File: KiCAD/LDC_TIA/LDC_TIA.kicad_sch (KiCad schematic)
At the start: 19 parts, among them J1 Conn_01x02_Pin, J2 Conn_01x06_Pin, J3 54-00166, Q1 BC817, SW1 SW_SPST, U1 OPA2197xDGK, U2 LM7805_TO220

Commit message: Initial Commit
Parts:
- J3: footprint JACK:TENSILITY_54-00166 -> Footprints:TENSILITY_54-00166
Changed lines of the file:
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@@
 			)
 		)
-		(property "Footprint" "JACK:TENSILITY_54-00166"
+		(property "Footprint" "Footprints:TENSILITY_54-00166"
 			(at 91.44 107.95 0)
 			(effects

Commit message: Done with Schematics V1
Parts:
- removed C1, C2: 10pF, Capacitor_SMD:C_0201_0603Metric, symbol Library:C
- removed C4: 0.33uF, Capacitor_SMD:C_0201_0603Metric, symbol Library:C
- removed C5: 0.1uF, Capacitor_SMD:C_0201_0603Metric, symbol Library:C
- removed J2: Conn_01x06_Pin, Connector_PinHeader_2.54mm:PinHeader_1x06_P2.54mm_Vertical, symbol Connector:Conn_01x06_Pin
- removed J3: 54-00166, Footprints:TENSILITY_54-00166, symbol Library:54-00166
- removed Q1: BC817, Package_TO_SOT_SMD:SOT-23, symbol Library:BC817
- removed R1: 2K, Resistor_THT:R_Axial_DIN0207_L6.3mm_D2.5mm_P7.62mm_Horizontal, symbol Library:R
- removed R2: 1K, Resistor_THT:R_Axial_DIN0207_L6.3mm_D2.5mm_P7.62mm_Horizontal, symbol Library:R
- removed R3: 62, Resistor_THT:R_Axial_DIN0309_L9.0mm_D3.2mm_P25.40mm_Horizontal, symbol Library:R
- removed R4, R5: 2k, Resistor_THT:R_Axial_DIN0204_L3.6mm_D1.6mm_P5.08mm_Horizontal, symbol Library:R
- removed SW1: SW_SPST, symbol Switch:SW_SPST
- removed U1: OPA2197xDGK, Package_SO:VSSOP-8_3x3mm_P0.65mm, symbol Library:OPA2197xDGK
- added C1: 0.1UF, FOOTPRINTS:CAP_UEP_5X11_NCH, symbol Device:C
- added C2, C7: 10pF, FOOTPRINTS:CAPRB250W50L400T250H550, symbol Device:C
- added C3, C6: 10pF, FOOTPRINTS:CAPRB250W50L400T250H550, symbol Device:C_Polarized_Small_US
- added C5: 0.33uF, FOOTPRINTS:CAP_UEP_5X11_NCH, symbol Device:C
- added J2: 54-00166, FOOTPRINTS:TENSILITY_54-00166, symbol 54-00166:54-00166
- added J5: Conn_01x07_Pin, Connector_PinHeader_2.54mm:PinHeader_1x07_P2.54mm_Vertical, symbol Connector:Conn_01x07_Pin
- added Q1: BC817, Package_TO_SOT_SMD:SOT-23, symbol potentiometer:BC817
- added R1: 2k, Resistor_THT:R_Axial_DIN0207_L6.3mm_D2.5mm_P7.62mm_Horizontal, symbol Device:R
- added R2: 1k, Resistor_THT:R_Axial_DIN0207_L6.3mm_D2.5mm_P7.62mm_Horizontal, symbol Device:R
- added R3: 62, Resistor_THT:R_Axial_DIN0309_L9.0mm_D3.2mm_P12.70mm_Horizontal, symbol Device:R
- added R4: 2K, Resistor_THT:R_Axial_DIN0207_L6.3mm_D2.5mm_P7.62mm_Horizontal, symbol potentiometer:R
- added R5: 2K, Resistor_THT:R_Axial_DIN0207_L6.3mm_D2.5mm_P7.62mm_Horizontal, symbol Device:R
- added S1: GPTS203211B, FOOTPRINTS:GPTS203211B, symbol GPTS203211B:GPTS203211B
- added U3: OPA2197xD, Package_SO:SOIC-8_3.9x4.9mm_P1.27mm, symbol Amplifier_Operational:OPA2197xD
- added U4: LTC1044, FOOTPRINTS:PDIP-8_N_LIT, symbol Regulator_SwitchedCapacitor:LTC1044
- RV1: footprint (none) -> FOOTPRINTS:potentiometer
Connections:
- net +VCC: now also C1.1, S1.1, U3.8 (V+), U4.8 (V+)
- net ANODE: now also J5.2 (Pin_2)
- net CATHODE: now also C2.1, J5.1 (Pin_1), R5.1, U3.6 (-)
- net GND: now also C1.2, C5.2, C6.1, C7.2, J2.B, J2.C, J5.6 (Pin_6), J5.7 (Pin_7), R1.2, R3.2, R4.2, U4.3 (GND)
- net VI: now also C5.1, J2.A
- net VOUT: now also C2.2, J5.3 (Pin_3), R5.2, U3.7
- net VR: now also J5.4 (Pin_4)
- net at D1.2 (A): now also S1.2
- net at J1.2 (Pin_2): now also Q1.3 (C)
- net at RV1.2: now also U3.3 (+)
- new net: Q1.2 (E), R2.2, R3.1
- new net: C7.1, R4.1, U3.5 (+)
- new net: Q1.1 (B), U3.1
- new net: C3.1, U4.2 (CAP+)
- new net: C3.2, U4.4 (CAP-)
- new net: R1.1, R2.1, U3.2 (-)
- new net -VCC: C6.2, J5.5 (Pin_5), U3.4 (V-), U4.5 (VOUT)
- no-connect marks 0 -> 3
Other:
- moved on the sheet: D1, J1, JP1, RV1, U2

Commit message: PCB layout
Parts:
- J3: renamed from J1; footprint Connector_Samtec_HPM_THT:Samtec_HPM-02-01-x-S_Straight_1x02_Pitch5.08mm -> Connector_PinHeader_2.54mm:PinHeader_1x02_P2.54mm_Vertical
- renumbered C7 to C1, C5 to C3, C3 to C4, C1 to C5, J2 to J1, J5 to J2, R4 to R1, R5 to R2, R1 to R3, R2 to R4, R3 to R5, U3 to U1, U4 to U2, U2 to U3
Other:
- moved on the sheet: U1C
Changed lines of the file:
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@@
 	)
 	(rectangle
-		(start 114.808 123.444)
-		(end 146.05 154.94)
+		(start 113.538 124.714)
+		(end 144.78 156.21)
 		(stroke
 			(width 0)
@@
 	)
 	(label "-VCC"
-		(at 128.27 144.78 270)
+		(at 127 146.05 270)
 		(effects
 			(font
@@
 	)
 	(label "+VCC"
-		(at 128.27 129.54 90)
+		(at 127 130.81 90)
 		(effects
 			(font
@@
 		(dnp no)
 		(fields_autoplaced yes)
-		(property "Reference" "#PWR04"
+		(property "Reference" "#PWR03"
 			(at 128.27 105.41 0)
 			(effects
@@
 			(project ""
 				(path "/c2e64472-a533-4958-9229-ae3f836cc80a"
-					(reference "#PWR04")
+					(reference "#PWR03")
 					(unit 1)
 				)
@@
 		(on_board yes)
 		(dnp no)
-		(property "Reference" "J5"
+		(property "Reference" "J2"
 			(at 166.37 125.73 0)
 			(effects
@@
 			(project ""
 				(path "/c2e64472-a533-4958-9229-ae3f836cc80a"
-					(reference "J5")
+					(reference "J2")
 					(unit 1)
 				)
@@
 		(dnp no)
 		(fields_autoplaced yes)
-		(property "Reference" "R3"
+		(property "Reference" "R5"
 			(at 266.7 99.0599 0)
 			(effects
@@
 			(project ""
 				(path "/c2e64472-a533-4958-9229-ae3f836cc80a"
-					(reference "R3")
+					(reference "R5")
 					(unit 1)
 				)
@@
 		(dnp no)
 		(fields_autoplaced yes)
-		(property "Reference" "C7"
+		(property "Reference" "C1"
 			(at 45.72 64.7699 0)
 			(effects
@@
 			(project ""
 				(path "/c2e64472-a533-4958-9229-ae3f836cc80a"
-					(reference "C7")
+					(reference "C1")
 					(unit 1)
 				)
@@
 		(dnp no)
 		(fields_autoplaced yes)
-		(property "Reference" "R5"
+		(property "Reference" "R2"
 			(at 74.93 71.12 90)
 			(effects
@@
 			(project ""
 				(path "/c2e64472-a533-4958-9229-ae3f836cc80a"
-					(reference "R5")
+					(reference "R2")
 					(unit 1)
 				)
@@
 		(on_board yes)
 		(dnp no)
-		(property "Reference" "C5"
+		(property "Reference" "C3"
 			(at 123.19 60.96 0)
 			(effects
@@
 			(project ""
 				(path "/c2e64472-a533-4958-9229-ae3f836cc80a"
-					(reference "C5")
+					(reference "C3")
 					(unit 1)
 				)
@@
 		(dnp no)
 		(fields_autoplaced yes)
-		(property "Reference" "C3"
+		(property "Reference" "C4"
 			(at 148.59 85.9281 0)
 			(effects
@@
 			(project ""
 				(path "/c2e64472-a533-4958-9229-ae3f836cc80a"
-					(reference "C3")
+					(reference "C4")
 					(unit 1)
 				)
@@
 		(on_board yes)
 		(dnp no)
-		(property "Reference" "J1"
+		(property "Reference" "J3"
 			(at 259.08 67.31 0)
 			(effects
@@
 			)
 		)
-		(property "Footprint" "Connector_Samtec_HPM_THT:Samtec_HPM-02-01-x-S_Straight_1x02_Pitch5.08mm"
+		(property "Footprint" "Connector_PinHeader_2.54mm:PinHeader_1x02_P2.54mm_Vertical"
 			(at 259.08 73.66 0)
 			(effects
@@
 			(project ""
 				(path "/c2e64472-a533-4958-9229-ae3f836cc80a"
-					(reference "J1")
+					(reference "J3")
 					(unit 1)
 				)
@@
 		(dnp no)
 		(fields_autoplaced yes)
-		(property "Reference" "#PWR03"
+		(property "Reference" "#PWR06"
 			(at 207.01 88.9 0)
 			(effects
@@
 			(project ""
 				(path "/c2e64472-a533-4958-9229-ae3f836cc80a"
-					(reference "#PWR03")
+					(reference "#PWR06")
 					(unit 1)
 				)
@@
 		(dnp no)
 		(fields_autoplaced yes)
-		(property "Reference" "#FLG02"
+		(property "Reference" "#FLG01"
 			(at 123.825 57.15 0)
 			(effects
@@
 			(project ""
 				(path "/c2e64472-a533-4958-9229-ae3f836cc80a"
-					(reference "#FLG02")
+					(reference "#FLG01")
 					(unit 1)
 				)
@@
 		(dnp no)
 		(fields_autoplaced yes)
-		(property "Reference" "U3"
+		(property "Reference" "U1"
 			(at 237.49 71.12 0)
 			(effects
@@
 			(project ""
 				(path "/c2e64472-a533-4958-9229-ae3f836cc80a"
-					(reference "U3")
+					(reference "U1")
 					(unit 1)
 				)
@@
 		(dnp no)
 		(fields_autoplaced yes)
-		(property "Reference" "#PWR06"
+		(property "Reference" "#PWR04"
 			(at 139.7 71.12 0)
 			(effects
@@
 			(project ""
 				(path "/c2e64472-a533-4958-9229-ae3f836cc80a"
-					(reference "#PWR06")
+					(reference "#PWR04")
 					(unit 1)
 				)
@@
 	(symbol
 		(lib_id "Amplifier_Operational:OPA2197xD")
-		(at 128.27 137.16 0)
+		(at 127 138.43 0)
 		(unit 3)
 		(exclude_from_sim no)
@@
 		(dnp no)
 		(fields_autoplaced yes)
-		(property "Reference" "U3"
-			(at 129.54 135.8899 0)
+		(property "Reference" "U1"
+			(at 128.27 137.1599 0)
 			(effects
 				(font
@@
 		)
 		(property "Value" "OPA2197xD"
-			(at 129.54 138.4299 0)
+			(at 128.27 139.6999 0)
 			(effects
 				(font
@@
 		)
 		(property "Footprint" "Package_SO:SOIC-8_3.9x4.9mm_P1.27mm"
-			(at 130.81 137.16 0)
+			(at 129.54 138.43 0)
 			(effects
 				(font
@@
 		)
 		(property "Datasheet" "http://www.ti.com/lit/ds/symlink/opa2197.pdf"
-			(at 134.62 133.35 0)
+			(at 133.35 134.62 0)
 			(effects
 				(font
@@
 		)
 		(property "Description" "Dual 36V, Precision, Rail-to-Rail Input/Output, Low Offset Voltage, Operational Amplifier, SOIC-8"
-			(at 128.27 137.16 0)
+			(at 127 138.43 0)
 			(effects
 				(font
@@
 			(project ""
 				(path "/c2e64472-a533-4958-9229-ae3f836cc80a"
-					(reference "U3")
+					(reference "U1")
 					(unit 3)
 				)
@@
 		(dnp no)
 		(fields_autoplaced yes)
-		(property "Reference" "R4"
+		(property "Reference" "R1"
 			(at 34.29 64.7699 0)
 			(effects
@@
 			(project ""
 				(path "/c2e64472-a533-4958-9229-ae3f836cc80a"
-					(reference "R4")
+					(reference "R1")
 					(unit 1)
 				)
@@
 		(dnp no)
 		(fields_autoplaced yes)
-		(property "Reference" "#PWR0102"
+		(property "Reference" "#PWR07"
 			(at 229.87 111.76 0)
 			(effects
@@
 			(project ""
 				(path "/c2e64472-a533-4958-9229-ae3f836cc80a"
-					(reference "#PWR0102")
+					(reference "#PWR07")
 					(unit 1)
 				)
@@
 		(dnp no)
 		(fields_autoplaced yes)
-		(property "Reference" "U4"
+		(property "Reference" "U2"
 			(at 128.27 71.12 0)
 			(effects
@@
 			(project ""
 				(path "/c2e64472-a533-4958-9229-ae3f836cc80a"
-					(reference "U4")
+					(reference "U2")
 					(unit 1)
 				)
@@
 		(dnp no)
 		(fields_autoplaced yes)
-		(property "Reference" "U2"
+		(property "Reference" "U3"
 			(at 139.7 50.8 0)
 			(effects
@@
 			(project ""
 				(path "/c2e64472-a533-4958-9229-ae3f836cc80a"
-					(reference "U2")
+					(reference "U3")
 					(unit 1)
 				)
@@
 		(dnp no)
 		(fields_autoplaced yes)
-		(property "Reference" "C1"
+		(property "Reference" "C5"
 			(at 153.67 59.6899 0)
 			(effects
@@
 			(project ""
 				(path "/c2e64472-a533-4958-9229-ae3f836cc80a"
-					(reference "C1")
+					(reference "C5")
 					(unit 1)
 				)
@@
 		(dnp no)
 		(fields_autoplaced yes)
-		(property "Reference" "#PWR01"
+		(property "Reference" "#PWR08"
 			(at 264.16 110.49 0)
 			(effects
@@
 			(project ""
 				(path "/c2e64472-a533-4958-9229-ae3f836cc80a"
-					(reference "#PWR01")
+					(reference "#PWR08")
 					(unit 1)
 				)
@@
 		(dnp no)
 		(fields_autoplaced yes)
-		(property "Reference" "J2"
+		(property "Reference" "J1"
 			(at 86.6803 127 0)
 			(effects
@@
 			(project ""
 				(path "/c2e64472-a533-4958-9229-ae3f836cc80a"
-					(reference "J2")
+					(reference "J1")
 					(unit 1)
 				)
@@
 		(dnp no)
 		(fields_autoplaced yes)
-		(property "Reference" "#PWR07"
+		(property "Reference" "#PWR01"
 			(at 36.83 76.2 0)
 			(effects
@@
 			(project ""
 				(path "/c2e64472-a533-4958-9229-ae3f836cc80a"
-					(reference "#PWR07")
+					(reference "#PWR01")
 					(unit 1)
 				)
@@
 		(dnp no)
 		(fields_autoplaced yes)
-		(property "Reference" "R1"
+		(property "Reference" "R3"
 			(at 232.41 100.3299 0)
 			(effects
@@
 			(project ""
 				(path "/c2e64472-a533-4958-9229-ae3f836cc80a"
-					(reference "R1")
+					(reference "R3")
 					(unit 1)
 				)
@@
 		(dnp no)
 		(fields_autoplaced yes)
-		(property "Reference" "R2"
+		(property "Reference" "R4"
 			(at 250.19 87.63 90)
 			(effects
@@
 			(project ""
 				(path "/c2e64472-a533-4958-9229-ae3f836cc80a"
-					(reference "R2")
+					(reference "R4")
 					(unit 1)
 				)
@@
 		(dnp no)
 		(fields_autoplaced yes)
-		(property "Reference" "U3"
+		(property "Reference" "U1"
 			(at 58.42 50.8 0)
 			(effects
@@
 			(project ""
 				(path "/c2e64472-a533-4958-9229-ae3f836cc80a"
-					(reference "U3")
+					(reference "U1")
 					(unit 2)
 				)
@@
 		(dnp no)
 		(fields_autoplaced yes)
-		(property "Reference" "#FLG01"
+		(property "Reference" "#FLG02"
 			(at 262.255 104.14 0)
 			(effects
@@
 			(project ""
 				(path "/c2e64472-a533-4958-9229-ae3f836cc80a"
-					(reference "#FLG01")
+					(reference "#FLG02")
 					(unit 1)
 				)

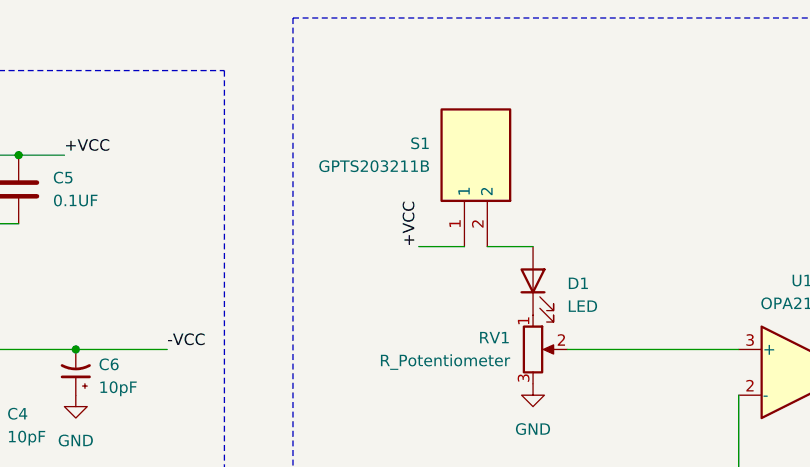
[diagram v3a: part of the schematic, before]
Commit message: PCB design and 3D Visualization
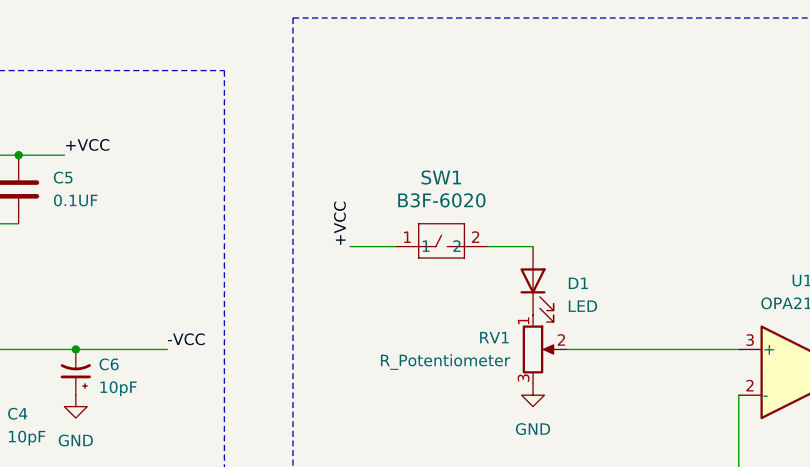
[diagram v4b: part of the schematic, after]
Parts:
- removed S1: GPTS203211B, FOOTPRINTS:GPTS203211B, symbol GPTS203211B:GPTS203211B
- added SW1: B3F-6020, FOOTPRINTS:SW_B3F-6020_OMR, symbol B3F_6020_tact_sw:B3F-6020
- R5: footprint Resistor_THT:R_Axial_DIN0309_L9.0mm_D3.2mm_P12.70mm_Horizontal -> FOOTPRINTS:RES_MRS25_VIS
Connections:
- net +VCC: now also SW1.1
- net at D1.2 (A): now also SW1.2
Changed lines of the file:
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@@
 	(wire
 		(pts
-			(xy 194.31 67.31) (xy 199.39 67.31)
+			(xy 186.69 67.31) (xy 191.77 67.31)
 		)
 		(stroke
@@
 	)
 	(label "+VCC"
-		(at 194.31 67.31 90)
+		(at 186.69 67.31 90)
 		(effects
 			(font
@@
 			)
 		)
-		(property "Footprint" "Resistor_THT:R_Axial_DIN0309_L9.0mm_D3.2mm_P12.70mm_Horizontal"
+		(property "Footprint" "FOOTPRINTS:RES_MRS25_VIS"
 			(at 262.382 100.33 90)
 			(effects
@@
 	)
 	(symbol
+		(lib_id "B3F_6020_tact_sw:B3F-6020")
+		(at 186.69 71.12 0)
+		(unit 1)
+		(exclude_from_sim no)
+		(in_bom yes)
+		(on_board yes)
+		(dnp no)
+		(fields_autoplaced yes)
+		(property "Reference" "SW1"
+			(at 196.85 59.69 0)
+			(effects
+				(font
+					(size 1.524 1.524)
+				)
+			)
+		)
+		(property "Value" "B3F-6020"
+			(at 196.85 62.23 0)
+			(effects
+				(font
+					(size 1.524 1.524)
+				)
+			)
+		)
+		(property "Footprint" "FOOTPRINTS:SW_B3F-6020_OMR"
+			(at 186.69 71.12 0)
+			(effects
+				(font
+					(size 1.27 1.27)
+					(italic yes)
+				)
+				(hide yes)
+			)
+		)
+		(property "Datasheet" "B3F-6020"
+			(at 186.69 71.12 0)
+			(effects
+				(font
+					(size 1.27 1.27)
+					(italic yes)
+				)
+				(hide yes)
+			)
+		)
+		(property "Description" ""
+			(at 186.69 71.12 0)
+			(effects
+				(font
+					(size 1.27 1.27)
+				)
+				(hide yes)
+			)
+		)
+		(pin "2"
+		)
+		(pin "1"
+		)
+		(instances
+			(project ""
+				(path "/c2e64472-a533-4958-9229-ae3f836cc80a"
+					(reference "SW1")
+					(unit 1)
+				)
+			)
+		)
+	)
+	(symbol
 		(lib_id "Device:C")
 		(at 41.91 66.04 0)
@@
 					(unit 1)
 				)
-			)
-		)
-	)
-	(symbol
-		(lib_id "GPTS203211B:GPTS203211B")
-		(at 201.93 67.31 270)
-		(mirror x)
-		(unit 1)
-		(exclude_from_sim no)
-		(in_bom yes)
-		(on_board yes)
-		(dnp no)
-		(property "Reference" "S1"
-			(at 195.58 55.8799 90)
-			(effects
-				(font
-					(size 1.27 1.27)
-				)
-				(justify right)
-			)
-		)
-		(property "Value" "GPTS203211B"
-			(at 195.58 58.4199 90)
-			(effects
-				(font
-					(size 1.27 1.27)
-				)
-				(justify right)
-			)
-		)
-		(property "Footprint" "FOOTPRINTS:GPTS203211B"
-			(at 107.01 50.8 0)
-			(effects
-				(font
-					(size 1.27 1.27)
-				)
-				(justify left top)
-				(hide yes)
-			)
-		)
-		(property "Datasheet" "http://switches-connectors-custom.cwind.com/Asset/GPTS203211BR2.pdf"
-			(at 7.01 50.8 0)
-			(effects
-				(font
-					(size 1.27 1.27)
-				)
-				(justify left top)
-				(hide yes)
-			)
-		)
-		(property "Description" "Pushbutton Switches SPST ON-OFF"
-			(at 201.93 67.31 0)
-			(effects
-				(font
-					(size 1.27 1.27)
-				)
-				(hide yes)
-			)
-		)
-		(property "Height" ""
-			(at -192.99 50.8 0)
-			(effects
-				(font
-					(size 1.27 1.27)
-				)
-				(justify left top)
-				(hide yes)
-			)
-		)
-		(property "Manufacturer_Name" "CW Industries"
-			(at -292.99 50.8 0)
-			(effects
-				(font
-					(size 1.27 1.27)
-				)
-				(justify left top)
-				(hide yes)
-			)
-		)
-		(property "Manufacturer_Part_Number" "GPTS203211B"
-			(at -392.99 50.8 0)
-			(effects
-				(font
-					(size 1.27 1.27)
-				)
-				(justify left top)
-				(hide yes)
-			)
-		)
-		(property "Mouser Part Number" "629-GPTS203211B"
-			(at -492.99 50.8 0)
-			(effects
-				(font
-					(size 1.27 1.27)
-				)
-				(justify left top)
-				(hide yes)
-			)
-		)
-		(property "Mouser Price/Stock" "https://www.mouser.co.uk/ProductDetail/CW-Industries/GPTS203211B?qs=sajaCoHCXPR%252BmLwibobs6Q%3D%3D"
-			(at -592.99 50.8 0)
-			(effects
-				(font
-					(size 1.27 1.27)
-				)
-				(justify left top)
-				(hide yes)
-			)
-		)
-		(property "Arrow Part Number" ""
-			(at -692.99 50.8 0)
-			(effects
-				(font
-					(size 1.27 1.27)
-				)
-				(justify left top)
-				(hide yes)
-			)
-		)
-		(property "Arrow Price/Stock" ""
-			(at -792.99 50.8 0)
-			(effects
-				(font
-					(size 1.27 1.27)
-				)
-				(justify left top)
-				(hide yes)
-			)
-		)
-		(pin "1"
-		)
-		(pin "2"
-		)
-		(instances
-			(project ""
-				(path "/c2e64472-a533-4958-9229-ae3f836cc80a"
-					(reference "S1")
-					(unit 1)
-				)

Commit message: PCB VOL 2
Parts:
- removed SW1: B3F-6020, FOOTPRINTS:SW_B3F-6020_OMR, symbol B3F_6020_tact_sw:B3F-6020
- added SW2: B3F-6020, SW_B3F-6020_OMR, symbol B3F_6020_tact_sw:B3F-6020
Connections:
- net +VCC: now also SW2.1
- net at D1.2 (A): now also SW2.2
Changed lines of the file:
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@@
-	(wire
-		(pts
-			(xy 186.69 67.31) (xy 191.77 67.31)
-		)
-		(stroke
-			(width 0)
-			(type default)
-		)
-	)
 	(wire
 		(pts
@@
 			(width 0)
 			(type default)
-		)
-	)
-	(label "+VCC"
-		(at 186.69 67.31 90)
-		(effects
-			(font
-				(size 1.27 1.27)
-			)
-			(justify left bottom)
 		)
 	)
@@
 			)
 			(justify left bottom)
+		)
+	)
+	(label "+VCC"
+		(at 191.77 67.31 180)
+		(effects
+			(font
+				(size 1.27 1.27)
+			)
+			(justify right bottom)
 		)
 	)
@@
 	)
 	(symbol
-		(lib_id "B3F_6020_tact_sw:B3F-6020")
-		(at 186.69 71.12 0)
-		(unit 1)
-		(exclude_from_sim no)
-		(in_bom yes)
-		(on_board yes)
-		(dnp no)
-		(fields_autoplaced yes)
-		(property "Reference" "SW1"
-			(at 196.85 59.69 0)
-			(effects
-				(font
-					(size 1.524 1.524)
-				)
-			)
-		)
-		(property "Value" "B3F-6020"
-			(at 196.85 62.23 0)
-			(effects
-				(font
-					(size 1.524 1.524)
-				)
-			)
-		)
-		(property "Footprint" "FOOTPRINTS:SW_B3F-6020_OMR"
-			(at 186.69 71.12 0)
-			(effects
-				(font
-					(size 1.27 1.27)
-					(italic yes)
-				)
-				(hide yes)
-			)
-		)
-		(property "Datasheet" "B3F-6020"
-			(at 186.69 71.12 0)
-			(effects
-				(font
-					(size 1.27 1.27)
-					(italic yes)
-				)
-				(hide yes)
-			)
-		)
-		(property "Description" ""
-			(at 186.69 71.12 0)
-			(effects
-				(font
-					(size 1.27 1.27)
-				)
-				(hide yes)
-			)
-		)
-		(pin "2"
-		)
-		(pin "1"
-		)
-		(instances
-			(project ""
-				(path "/c2e64472-a533-4958-9229-ae3f836cc80a"
-					(reference "SW1")
-					(unit 1)
-				)
-			)
-		)
-	)
-	(symbol
 		(lib_id "Device:C")
 		(at 41.91 66.04 0)
@@
 					(unit 1)
 				)
+			)
+		)
+	)
+	(symbol
+		(lib_name "B3F-6020_1")
+		(lib_id "B3F_6020_tact_sw:B3F-6020")
+		(at 186.69 71.12 0)
+		(unit 1)
+		(exclude_from_sim no)
+		(in_bom yes)
+		(on_board yes)
+		(dnp no)
+		(fields_autoplaced yes)
+		(property "Reference" "SW2"
+			(at 196.85 59.69 0)
+			(effects
+				(font
+					(size 1.524 1.524)
+				)
+			)
+		)
+		(property "Value" "B3F-6020"
+			(at 196.85 62.23 0)
+			(effects
+				(font
+					(size 1.524 1.524)
+				)
+			)
+		)
+		(property "Footprint" "SW_B3F-6020_OMR"
+			(at 186.69 71.12 0)
+			(effects
+				(font
+					(size 1.27 1.27)
+					(italic yes)
+				)
+				(hide yes)
+			)
+		)
+		(property "Datasheet" "B3F-6020"
+			(at 186.69 71.12 0)
+			(effects
+				(font
+					(size 1.27 1.27)
+					(italic yes)
+				)
+				(hide yes)
+			)
+		)
+		(property "Description" ""
+			(at 186.69 71.12 0)
+			(effects
+				(font
+					(size 1.27 1.27)
+				)
+				(hide yes)
+			)
+		)
+		(pin "2"
+		)
+		(pin "1"
+		)
+		(instances
+			(project ""
+				(path "/c2e64472-a533-4958-9229-ae3f836cc80a"
+					(reference "SW2")
+					(unit 1)
+				)

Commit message: PCB_LAYOUT_VOL2
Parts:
- SW2: footprint SW_B3F-6020_OMR -> FOOTPRINTS:SW_B3F-6020_OMR
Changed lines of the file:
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@@
 	)
 	(symbol
-		(lib_name "B3F-6020_1")
 		(lib_id "B3F_6020_tact_sw:B3F-6020")
 		(at 186.69 71.12 0)
@@
 			)
 		)
-		(property "Footprint" "SW_B3F-6020_OMR"
+		(property "Footprint" "FOOTPRINTS:SW_B3F-6020_OMR"
 			(at 186.69 71.12 0)
 			(effects

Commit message: schematic v5
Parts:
- R5: value 62 -> 100
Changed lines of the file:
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@@
 			)
 		)
-		(property "Value" "62"
+		(property "Value" "100"
 			(at 266.7 101.5999 0)
 			(effects
